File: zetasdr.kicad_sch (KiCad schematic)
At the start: 47 parts, among them J2 USB_B, J5 Antenna, J6 AudioJack3_SwitchTR, Q1 BC547C, U1 74AHC1G04, U2 74HC74, U3 4052, U4 NE5532

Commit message: add connectors for picoscope
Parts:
- removed J6: AudioJack3_SwitchTR, Connector_Audio:Jack_3.5mm_CUI_SJ1-3525N_Horizontal, symbol Connector_Audio:AudioJack3_SwitchTR
- removed R10, R9: 4k7, Resistor_SMD:R_0805_2012Metric_Pad1.20x1.40mm_HandSolder, symbol Device:R
- removed RV1: 50k, Potentiometer_THT:Potentiometer_Piher_T-16H_Single_Horizontal, symbol Device:R_Potentiometer
- added J1: Output I, Connector_Coaxial:SMA_Amphenol_901-143_Horizontal, symbol Connector:Conn_Coaxial
- added J3: Output Q, Connector_Coaxial:SMA_Amphenol_901-143_Horizontal, symbol Connector:Conn_Coaxial
- added J4: Input AWG, Connector_Coaxial:SMA_Amphenol_901-143_Horizontal, symbol Connector:Conn_Coaxial
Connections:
- net GND: now also J1.2 (Ext), J3.2 (Ext), J4.2 (Ext)
- net at C4.1, R8.1: now also J4.1 (In)
- net at C14.2: now also J1.1 (In)
- net at C15.2: now also J3.1 (In)
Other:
- moved on the sheet: C13

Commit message: first layout
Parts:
- added H3: MountingHole_Pad, MountingHole:MountingHole_3.2mm_M3_Pad, symbol Mechanical:MountingHole_Pad
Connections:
- net GND: now also H3.1
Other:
- moved on the sheet: C13, C16, C20, C3, C9, D1, R11, R7, U2C

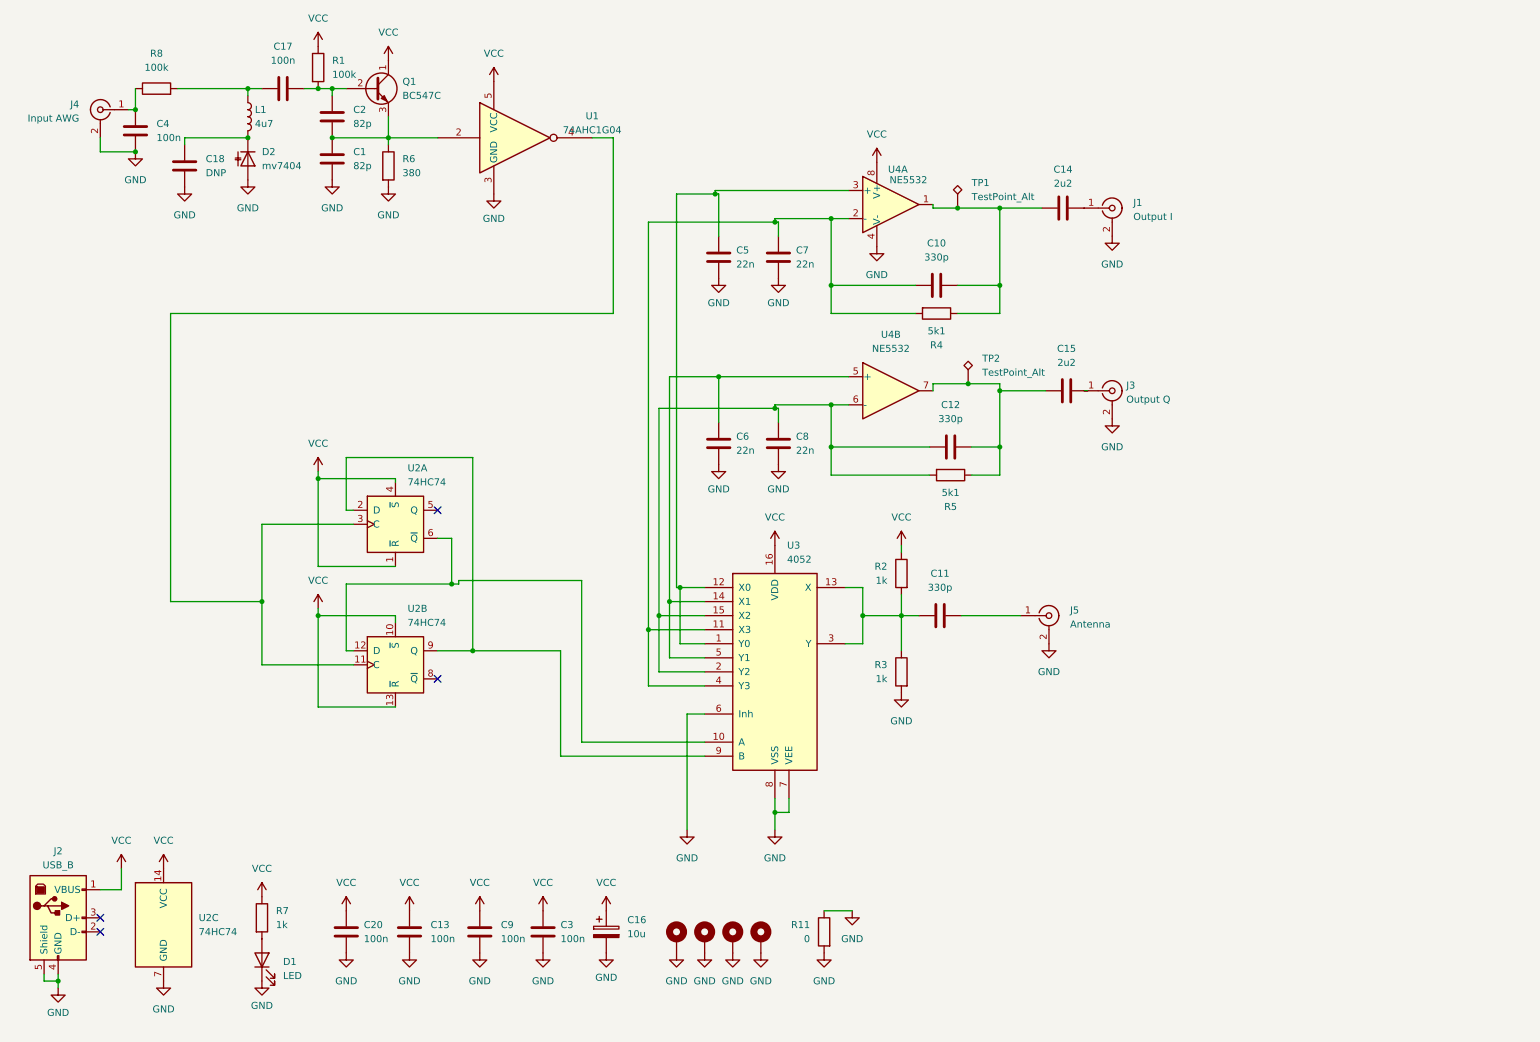
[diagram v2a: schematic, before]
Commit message: 80m filter & new layout
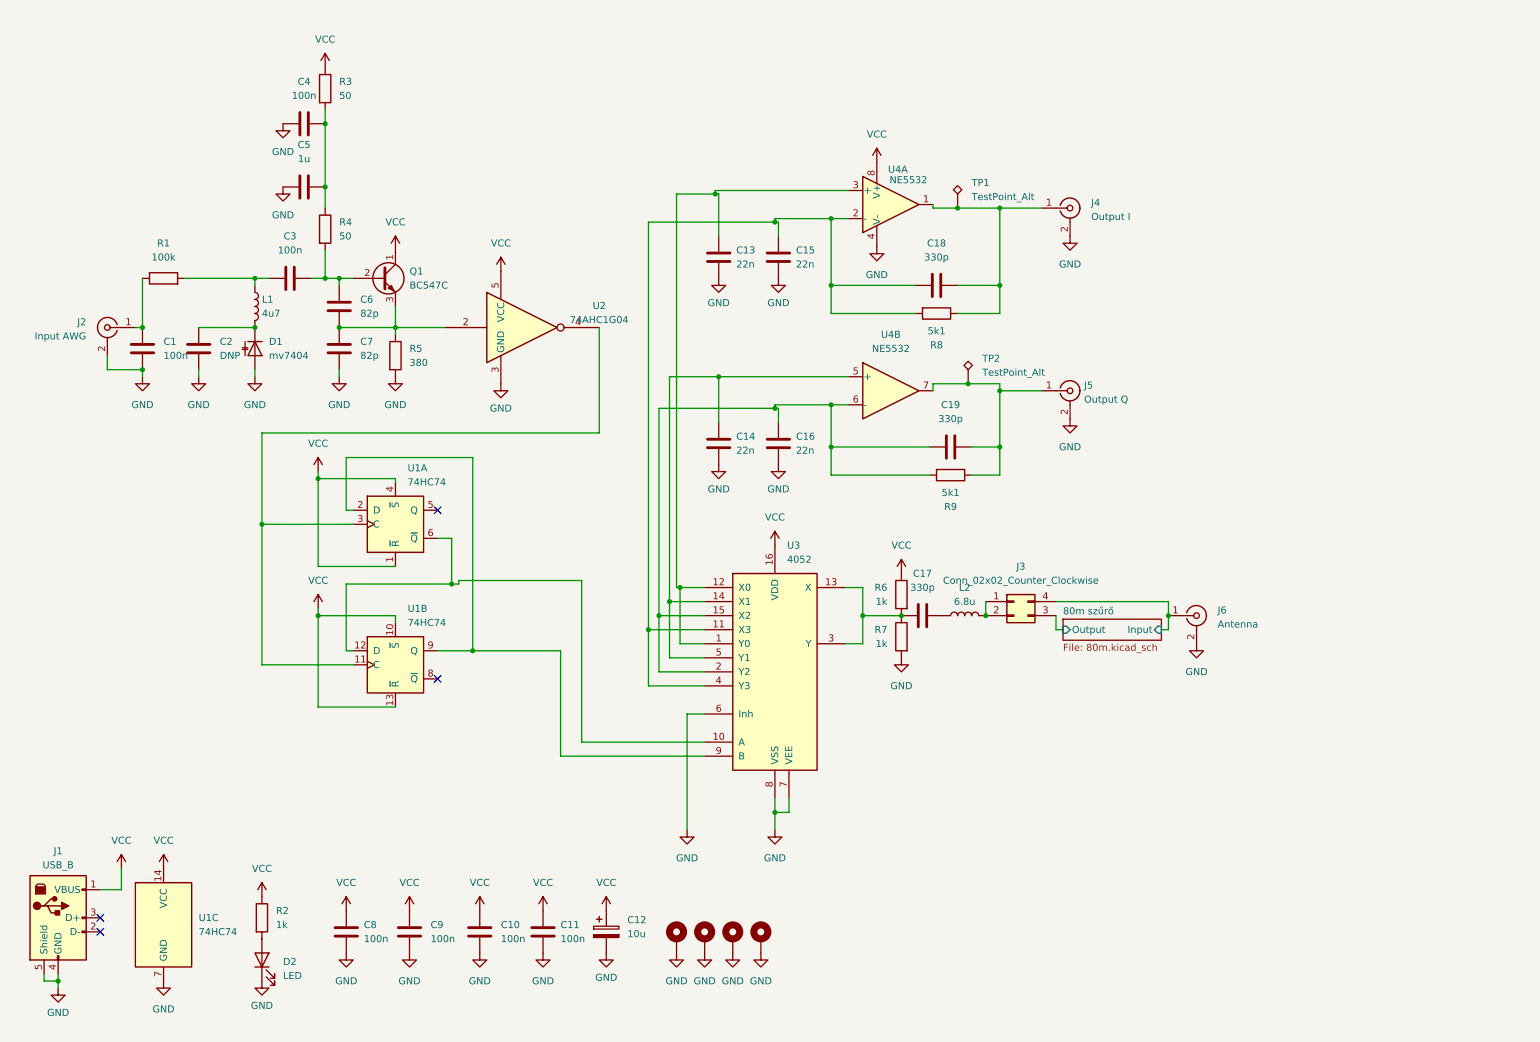
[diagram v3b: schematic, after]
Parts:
- removed C14, C15: 2u2, Capacitor_SMD:C_0805_2012Metric_Pad1.18x1.45mm_HandSolder, symbol Device:C
- removed R11: 0, Resistor_THT:R_Axial_DIN0309_L9.0mm_D3.2mm_P12.70mm_Horizontal, symbol Device:R
- added C4: 100n, Capacitor_SMD:C_0805_2012Metric_Pad1.18x1.45mm_HandSolder, symbol Device:C
- added C5: 1u, Capacitor_SMD:C_0805_2012Metric_Pad1.18x1.45mm_HandSolder, symbol Device:C
- added J3: Conn_02x02_Counter_Clockwise, Connector_PinHeader_2.54mm:PinHeader_2x02_P2.54mm_Vertical, symbol Connector_Generic:Conn_02x02_Counter_Clockwise
- added L2: 6.8u, Inductor_SMD:L_1210_3225Metric_Pad1.42x2.65mm_HandSolder, symbol Device:L
- added R3: 50, Resistor_THT:R_Axial_DIN0204_L3.6mm_D1.6mm_P2.54mm_Vertical, symbol Device:R
- J2: renamed from J4; footprint Connector_Coaxial:SMA_Amphenol_901-143_Horizontal -> Connector_Coaxial:BNC_TEConnectivity_1478035_Horizontal
- J4: renamed from J1; footprint Connector_Coaxial:SMA_Amphenol_901-143_Horizontal -> Connector_Coaxial:BNC_TEConnectivity_1478035_Horizontal
- J5: renamed from J3; footprint Connector_Coaxial:SMA_Amphenol_901-143_Horizontal -> Connector_Coaxial:BNC_TEConnectivity_1478035_Horizontal
- R4: renamed from R1; value 100k -> 50
- R9: renamed from R5; footprint Resistor_THT:R_Axial_DIN0204_L3.6mm_D1.6mm_P5.08mm_Horizontal -> Resistor_THT:R_Axial_DIN0204_L3.6mm_D1.6mm_P2.54mm_Vertical
- renumbered C4 to C1, C9 to C10, C3 to C11, C16 to C12, C5 to C13, C6 to C14, C7 to C15, C8 to C16, C11 to C17, C10 to C18, C12 to C19, C18 to C2, C17 to C3, C2 to C6, C1 to C7, C20 to C8, C13 to C9, D2 to D1, D1 to D2, H4 to H1, H3 to H2, H1 to H3, H2 to H4, J2 to J1, J5 to J6, R8 to R1, R7 to R2, R6 to R5, R2 to R6, R3 to R7, R4 to R8, U2 to U1, U1 to U2
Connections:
- net GND: now also C4.1, C5.1
- net VCC: now also R3.1; no longer R4.1
- net at C18.2, R8.1, TP1.1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: now also J4.1 (In)
- net at C19.2, R9.1, TP2.1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: now also J5.1 (In)
- net at C17.2: now also L2.1; no longer J6.1 (In)
- new net: J3.1 (Pin_1), J3.2 (Pin_2), L2.2
- new net: C4.2, C5.2, R3.2, R4.1
- new net 80m szűrő/Input: J3.4 (Pin_4), J6.1 (In)
- new net 80m szűrő/Output: J3.3 (Pin_3)
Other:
- added sheet 80m szűrő (80m.kicad_sch)
- moved on the sheet: C1, C17, C2, C3, C6, C7, D1, J2, J4, J5, J6, L1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

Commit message: bom
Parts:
- removed L2: 6.8u, Inductor_SMD:L_1210_3225Metric_Pad1.42x2.65mm_HandSolder, symbol Device:L
- C1, C10, C11, C3, C4, C9: RET (none) -> CC0805KRX7R8BB104
- C12: RET (none) -> SE063M0010B2F-0511
- C13, C14, C15, C16: RET (none) -> NCD223M50Z5U2.5MMLSF
- C17: value 330p -> 1n; RET (none) -> NCD102K50Y5PTR2.5MMLSF
- C18, C19: RET (none) -> NCD331K50Y5PTR2.5MMLSF
- C2: RET (none) -> -; now not fitted
- C5: Mouser (none) -> 963-MLASH21GBB5105KT; RET (none) -> -
- C6, C7: RET (none) -> CC0805JRNPO9BN820
- C8: footprint Capacitor_THT:C_Disc_D3.0mm_W1.6mm_P2.50mm -> Capacitor_SMD:C_0805_2012Metric_Pad1.18x1.45mm_HandSolder; RET (none) -> CC0805KRX7R8BB104
- D1: RET (none) -> ?
- D2: RET (none) -> LTL-4221NLC
- H1, H2, H3, H4: RET (none) -> -
- J1: RET (none) -> UJ2-BH-W1-TH
- J2, J4, J5: footprint Connector_Coaxial:BNC_TEConnectivity_1478035_Horizontal -> Connector_Coaxial:BNC_Amphenol_B6252HB-NPP3G-50_Horizontal; RET (none) -> UG1094PR
- J3: RET (none) -> DIS-250-S037-55
- J6: RET (none) -> SMA6252A2-3GT50G-50
- L1: RET (none) -> NLQ35M4R7TRF
- Q1: RET (none) -> BC547CBK
- R1: RET (none) -> RC0805FR-07100KL
- R2: RET (none) -> RC0805JR-071KL
- R3, R4: value 50 -> 50k; RET (none) -> MF0207FTE52-51K
- R5: value 380 -> 380 (383); Mouser (none) -> 279-LR1F383R; RET (none) -> -
- R6, R7: RET (none) -> CFR-25JT-52-1K
- R8, R9: RET (none) -> CFR-25JT-52-5K1
- U1: RET (none) -> CD74HC74E
- U2: footprint Package_TO_SOT_SMD:SOT-23-5_HandSoldering -> Package_TO_SOT_SMD:SOT-353_SC-70-5_Handsoldering; Mouser (none) -> 621-74AHC1G04SE-7; RET (none) -> -
- U3: Mouser (none) -> 595-CD4052BEE4; RET (none) -> -
- U4: RET (none) -> NE5532AP
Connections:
- net at J3.1 (Pin_1), J3.2 (Pin_2): now also C17.2

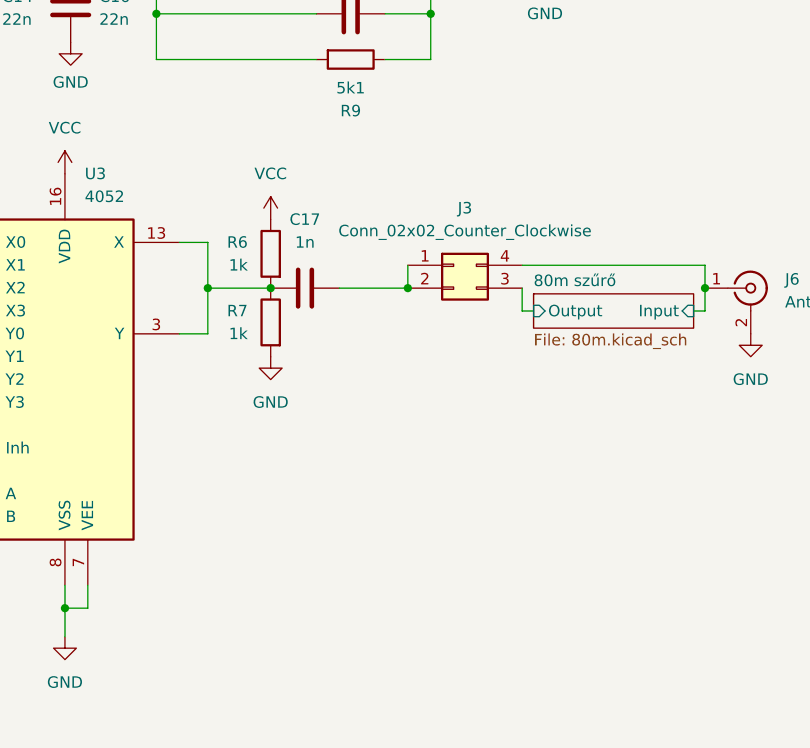
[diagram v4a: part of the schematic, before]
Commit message: rf bias filtering
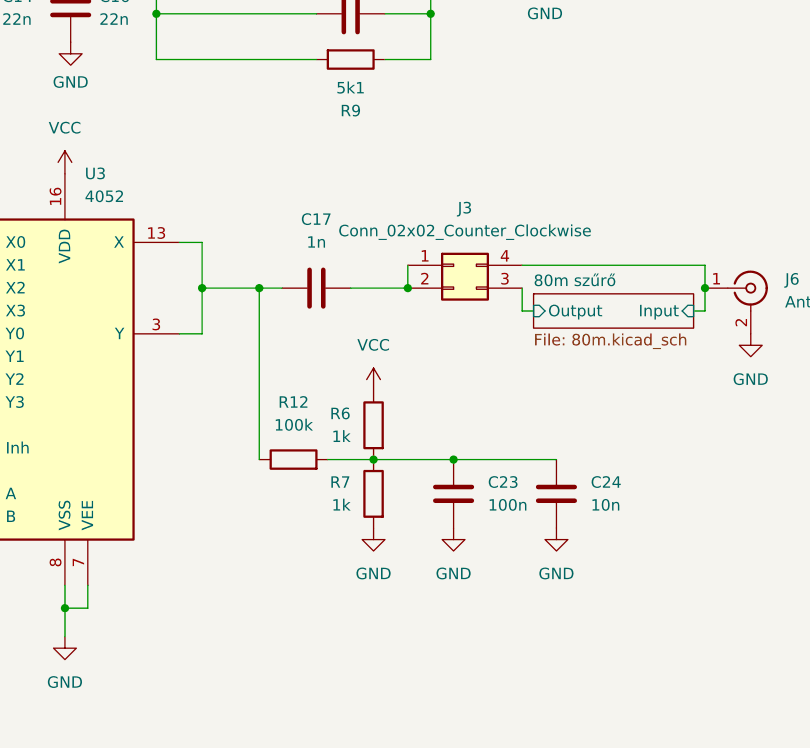
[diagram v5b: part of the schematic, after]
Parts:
- added C23: 100n, Capacitor_SMD:C_0805_2012Metric_Pad1.18x1.45mm_HandSolder, symbol Device:C
- added C24: 10n, Capacitor_SMD:C_0603_1608Metric_Pad1.08x0.95mm_HandSolder, symbol Device:C
- added R12: 100k, Resistor_SMD:R_0805_2012Metric_Pad1.20x1.40mm_HandSolder, symbol Device:R
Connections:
- net GND: now also C23.2, C24.2
- net at C17.1, U3.13 (X), U3.3 (Y): now also R12.1; no longer R6.2, R7.1
- new net: C23.1, C24.1, R12.2, R6.2, R7.1
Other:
- moved on the sheet: C17, R6, R7

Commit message: bias tee
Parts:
- added C25: 10n, Capacitor_SMD:C_0603_1608Metric_Pad1.08x0.95mm_HandSolder, symbol Device:C
- added J7, J8: Conn_02x02_Counter_Clockwise, Connector_PinHeader_2.54mm:PinHeader_2x02_P2.54mm_Vertical, symbol Connector_Generic:Conn_02x02_Counter_Clockwise
- added L2: 22u, Inductor_THT:L_Axial_L9.5mm_D4.0mm_P12.70mm_Horizontal_Fastron_SMCC, symbol Device:L
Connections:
- net 80m szűrő/Input: now also J8.3 (Pin_3), J8.4 (Pin_4); no longer J6.1 (In)
- net GND: now also J7.2 (Pin_2)
- net VCC: now also J7.4 (Pin_4)
- new net: J7.1 (Pin_1), L2.1
- new net: C25.2, J6.1 (In), J8.1 (Pin_1), L2.2
- new net: C25.1, J8.2 (Pin_2)
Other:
- moved on the sheet: J6

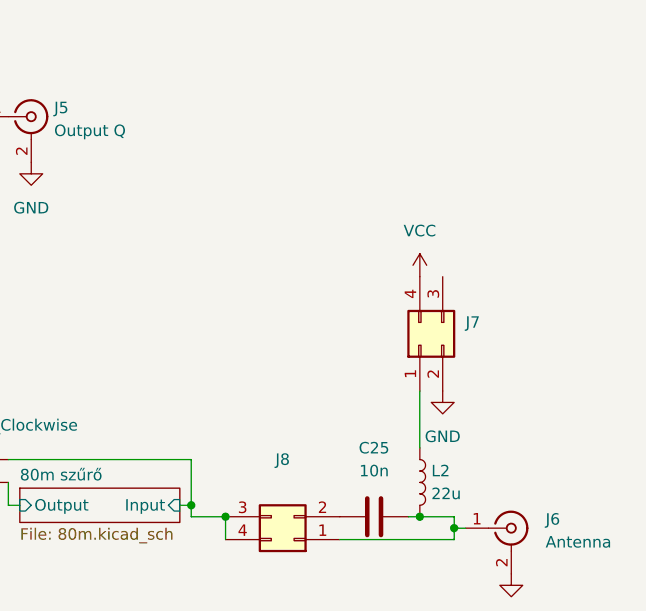
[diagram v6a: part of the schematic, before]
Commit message: bias tee power filter
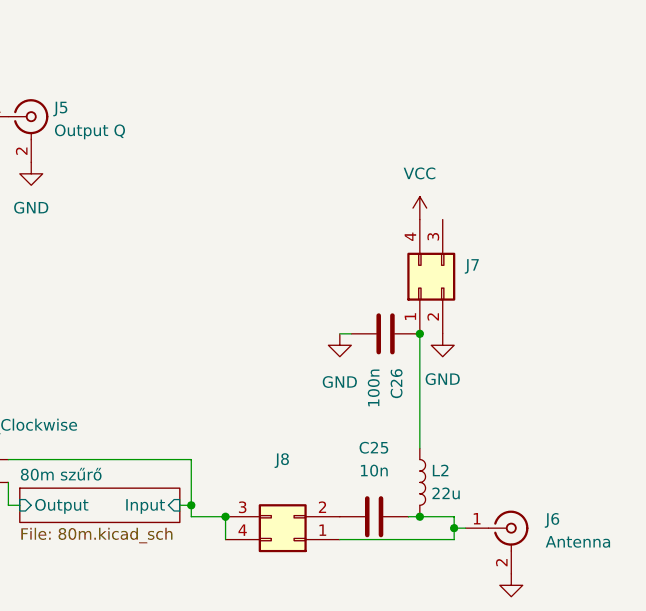
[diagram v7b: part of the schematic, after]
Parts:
- added C26: 100n, Capacitor_SMD:C_0805_2012Metric_Pad1.18x1.45mm_HandSolder, symbol Device:C
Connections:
- net GND: now also C26.2
- net at J7.1 (Pin_1), L2.1: now also C26.1
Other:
- moved on the sheet: J7
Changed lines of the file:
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@@
 	)
 	(junction
+		(at 246.38 106.68)
+		(diameter 0)
+		(color 0 0 0 0)
+	)
+	(junction
 		(at 190.5 63.5)
 		(diameter 0)
@@
 	(wire
 		(pts
+			(xy 246.38 106.68) (xy 246.38 119.38)
+		)
+		(stroke
+			(width 0)
+			(type default)
+		)
+	)
+	(wire
+		(pts
 			(xy 57.15 90.17) (xy 57.15 106.68)
 		)
@@
 	(wire
 		(pts
+			(xy 237.49 106.68) (xy 238.76 106.68)
+		)
+		(stroke
+			(width 0)
+			(type default)
+		)
+	)
+	(wire
+		(pts
 			(xy 132.08 46.99) (xy 139.065 46.99)
 		)
@@
 	(wire
 		(pts
-			(xy 246.38 113.03) (xy 246.38 119.38)
-		)
-		(stroke
-			(width 0)
-			(type default)
-		)
-	)
-	(wire
-		(pts
 			(xy 88.9 109.22) (xy 91.44 109.22)
 		)
@@
 	(symbol
 		(lib_id "Device:C")
+		(at 242.57 106.68 270)
+		(unit 1)
+		(exclude_from_sim no)
+		(in_bom yes)
+		(on_board yes)
+		(dnp no)
+		(fields_autoplaced yes)
+		(property "Reference" "C26"
+			(at 243.8401 110.49 0)
+			(effects
+				(font
+					(size 1.27 1.27)
+				)
+				(justify left)
+			)
+		)
+		(property "Value" "100n"
+			(at 241.3001 110.49 0)
+			(effects
+				(font
+					(size 1.27 1.27)
+				)
+				(justify left)
+			)
+		)
+		(property "Footprint" "Capacitor_SMD:C_0805_2012Metric_Pad1.18x1.45mm_HandSolder"
+			(at 238.76 107.6452 0)
+			(effects
+				(font
+					(size 1.27 1.27)
+				)
+				(hide yes)
+			)
+		)
+		(property "Datasheet" "~"
+			(at 242.57 106.68 0)
+			(effects
+				(font
+					(size 1.27 1.27)
+				)
+				(hide yes)
+			)
+		)
+		(property "Description" "Unpolarized capacitor"
+			(at 242.57 106.68 0)
+			(effects
+				(font
+					(size 1.27 1.27)
+				)
+				(hide yes)
+			)
+		)
+		(pin "1"
+		)
+		(pin "2"
+		)
+		(instances
+			(project "zetasdr"
+				(path "/de94b6ce-b3ae-4dfb-9d41-6753717007aa"
+					(reference "C26")
+					(unit 1)
+				)
+			)
+		)
+	)
+	(symbol
+		(lib_id "Device:C")
 		(at 150.495 92.075 0)
 		(unit 1)
@@
 	(symbol
 		(lib_id "power:GND")
+		(at 237.49 106.68 0)
+		(unit 1)
+		(exclude_from_sim no)
+		(in_bom yes)
+		(on_board yes)
+		(dnp no)
+		(fields_autoplaced yes)
+		(property "Reference" "#PWR056"
+			(at 237.49 113.03 0)
+			(effects
+				(font
+					(size 1.27 1.27)
+				)
+				(hide yes)
+			)
+		)
+		(property "Value" "GND"
+			(at 237.49 112.0775 0)
+			(effects
+				(font
+					(size 1.27 1.27)
+				)
+			)
+		)
+		(property "Footprint" ""
+			(at 237.49 106.68 0)
+			(effects
+				(font
+					(size 1.27 1.27)
+				)
+				(hide yes)
+			)
+		)
+		(property "Datasheet" ""
+			(at 237.49 106.68 0)
+			(effects
+				(font
+					(size 1.27 1.27)
+				)
+				(hide yes)
+			)
+		)
+		(property "Description" ""
+			(at 237.49 106.68 0)
+			(effects
+				(font
+					(size 1.27 1.27)
+				)
+			)
+		)
+		(pin "1"
+		)
+		(instances
+			(project "zetasdr"
+				(path "/de94b6ce-b3ae-4dfb-9d41-6753717007aa"
+					(reference "#PWR056")
+					(unit 1)
+				)
+			)
+		)
+	)
+	(symbol
+		(lib_id "power:GND")
 		(at 72.39 184.15 0)
 		(unit 1)
@@
 		(lib_name "VCC_1")
 		(lib_id "power:VCC")
-		(at 246.38 100.33 0)
+		(at 246.38 93.98 0)
 		(unit 1)
 		(exclude_from_sim no)
@@
 		(fields_autoplaced yes)
 		(property "Reference" "#PWR055"
-			(at 246.38 104.14 0)
+			(at 246.38 97.79 0)
 			(effects
 				(font
@@
 		)
 		(property "Value" "VCC"
-			(at 246.38 95.25 0)
+			(at 246.38 88.9 0)
 			(effects
 				(font
@@
 		)
 		(property "Footprint" ""
-			(at 246.38 100.33 0)
+			(at 246.38 93.98 0)
 			(effects
 				(font
@@
 		)
 		(property "Datasheet" ""
-			(at 246.38 100.33 0)
+			(at 246.38 93.98 0)
 			(effects
 				(font
@@
 		)
 		(property "Description" "Power symbol creates a global label with name \"VCC\""
-			(at 246.38 100.33 0)
+			(at 246.38 93.98 0)
 			(effects
 				(font
@@
 		(lib_name "GND_1")
 		(lib_id "power:GND")
-		(at 248.92 113.03 0)
+		(at 248.92 106.68 0)
 		(unit 1)
 		(exclude_from_sim no)
@@
 		(fields_autoplaced yes)
 		(property "Reference" "#PWR054"
-			(at 248.92 119.38 0)
+			(at 248.92 113.03 0)
 			(effects
 				(font
@@
 		)
 		(property "Value" "GND"
-			(at 248.92 118.11 0)
+			(at 248.92 111.76 0)
 			(effects
 				(font
@@
 		)
 		(property "Footprint" ""
-			(at 248.92 113.03 0)
+			(at 248.92 106.68 0)
 			(effects
 				(font
@@
 		)
 		(property "Datasheet" ""
-			(at 248.92 113.03 0)
+			(at 248.92 106.68 0)
 			(effects
 				(font
@@
 		)
 		(property "Description" "Power symbol creates a global label with name \"GND\" , ground"
-			(at 248.92 113.03 0)
+			(at 248.92 106.68 0)
 			(effects
 				(font
@@
 	(symbol
 		(lib_id "Connector_Generic:Conn_02x02_Counter_Clockwise")
-		(at 246.38 107.95 90)
+		(at 246.38 101.6 90)
 		(unit 1)
 		(exclude_from_sim no)
@@
 		(fields_autoplaced yes)
 		(property "Reference" "J7"
-			(at 251.46 105.4099 90)
+			(at 251.46 99.0599 90)
 			(effects
 				(font
@@
 		)
 		(property "Value" "Conn_02x02_Counter_Clockwise"
-			(at 251.46 107.9499 90)
+			(at 251.46 101.5999 90)
 			(effects
 				(font
@@
 		)
 		(property "Footprint" "Connector_PinHeader_2.54mm:PinHeader_2x02_P2.54mm_Vertical"
-			(at 246.38 107.95 0)
+			(at 246.38 101.6 0)
 			(effects
 				(font
@@
 		)
 		(property "Datasheet" "~"
-			(at 246.38 107.95 0)
+			(at 246.38 101.6 0)
 			(effects
 				(font
@@
 		)
 		(property "Description" "Generic connector, double row, 02x02, counter clockwise pin numbering scheme (similar to DIP package numbering), script generated (kicad-library-utils/schlib/autogen/connector/)"
-			(at 246.38 107.95 0)
+			(at 246.38 101.6 0)
 			(effects
 				(font
@@
 		)
 		(property "Mouser" ""
-			(at 246.38 107.95 0)
+			(at 246.38 101.6 0)
 			(effects
 				(font
@@
 		)
 		(property "RET" "DIS-250-S037-55"
-			(at 246.38 107.95 0)
+			(at 246.38 101.6 0)
 			(effects
 				(font
